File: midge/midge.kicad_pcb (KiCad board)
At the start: 2 copper layers, 121.1 x 83.6 mm, 21 parts, among them SW1 SW_PUSH, SW10 SW_PUSH, SW11 SW_PUSH, SW12 SW_PUSH, SW13 SW_PUSH, SW14 SW_PUSH, SW15 SW_PUSH, SW2 SW_PUSH, SW3 SW_PUSH, SW4 SW_PUSH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

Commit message: Renamed Knott to Midge.
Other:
- board text added: "Midge v0.2.1 https://github.com/jimmerricks/bugs"
- board text removed: "Knott v0.2 https://github.com/jimmerricks/bugs"
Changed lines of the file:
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@@
   (paper "A4")
   (title_block
-    (title "Knott")
-    (date "2021-08-18")
-    (rev "0.2")
+    (title "Midge")
+    (date "2021-09-20")
+    (rev "0.2.1")
     (company "jmnw")
   )
@@
   (gr_line (start 126.027238 50.063266) (end 126.001582 59.553053) (layer "Edge.Cuts") (width 0.15))
   (gr_arc (start 128.001577 59.553052) (end 126.001582 59.553053) (angle -90) (layer "Edge.Cuts") (width 0.15))
-  (gr_text "Knott v0.2\nhttps://github.com/jimmerricks/bugs" (at 139.61 94.87 90) (layer "F.SilkS")
+  (gr_text "Midge v0.2.1\nhttps://github.com/jimmerricks/bugs" (at 139.61 94.87 90) (layer "F.SilkS")
     (effects (font (size 1 1) (thickness 0.12)) (justify left))
   )

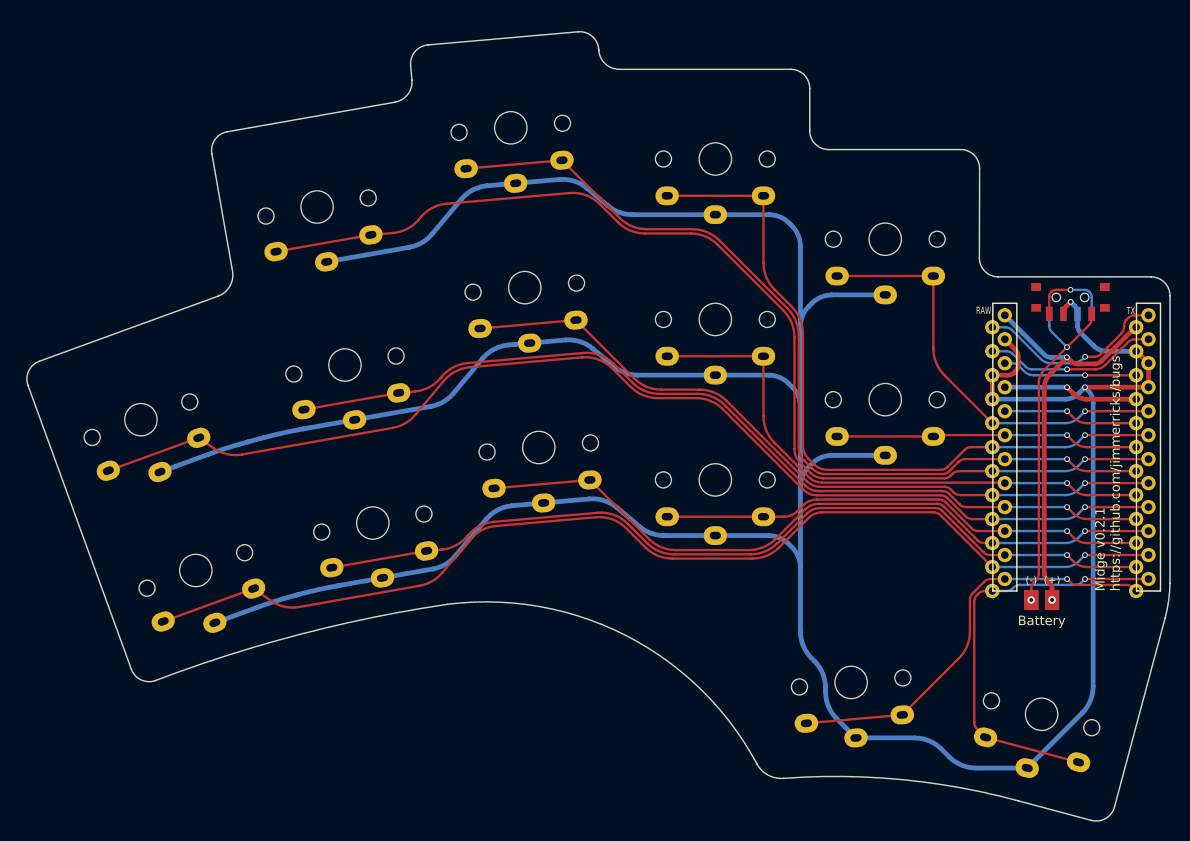
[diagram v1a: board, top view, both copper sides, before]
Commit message: Updated the Midge to the jumper pro micro footprint, breaking the pin order.
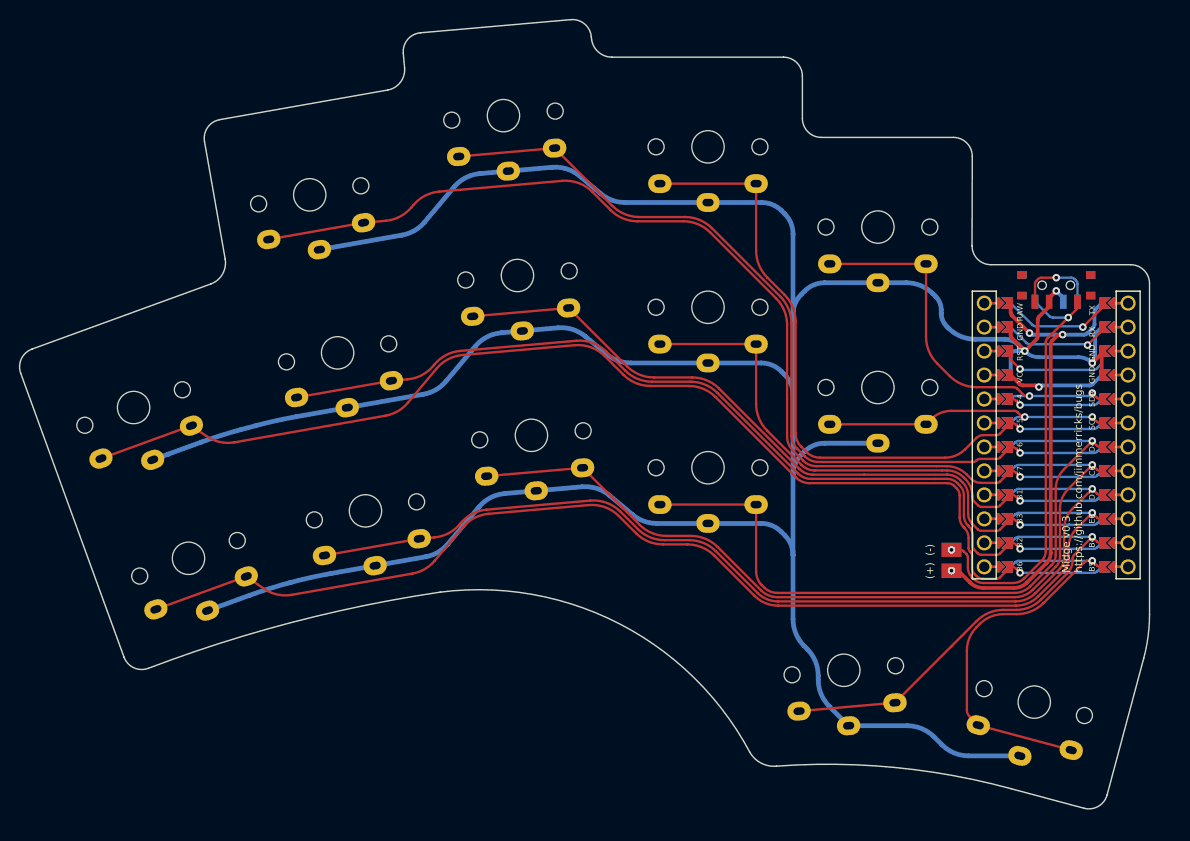
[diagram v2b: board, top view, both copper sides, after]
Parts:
- U1: footprint bugs:ProMicro_reversible -> bugs:ProMicro_jumpers
- moved BT1 10.4 mm to (123.0, 91.6), turned to 90 degrees
- moved U1 2.35 mm to (134.1, 78.3)
- moved PSW1 1.98 mm to (134.1, 62.4)
- moved SW10 1.51 mm to (115.2, 73.3)
- moved Ref** 1.51 mm to (54.3, 66.0)
- moved SW1 1.51 mm to (36.4, 75.4)
- moved SW3 1.51 mm to (75.6, 44.5)
- moved SW5 1.51 mm to (115.2, 56.3)
- moved Ref** 1.51 mm to (57.3, 82.7)
- moved SW6 1.51 mm to (42.2, 91.4)
- moved SW11 1.51 mm to (61.0, 86.3)
- moved SW2 1.51 mm to (55.1, 52.9)
- moved SW9 1.51 mm to (97.2, 64.8)
- moved Ref** 1.51 mm to (112.3, 56.1)
- moved SW13 1.51 mm to (97.2, 81.8)
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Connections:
- U1 pad 10: switch12 -> switch6
- U1 pad 11: switch6 -> switch14
- U1 pad 13: switch14 -> switch1
- U1 pad 14: switch11 -> switch7
- U1 pad 15: switch13 -> switch8
- U1 pad 16: switch7 -> switch9
- U1 pad 17: switch9 -> switch2
- U1 pad 19: switch10 -> switch4
- U1 pad 6: switch4 -> switch10
- U1 pad 7: switch2 -> switch13
- U1 pad 8: switch8 -> switch12
- U1 pad 9: switch1 -> switch11
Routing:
- net GND: track 379.2 -> 344.2 mm, vias 2 -> 3
- net switch13: track 52.1 -> 75.8 mm
- net switch12: track 76.1 -> 89.0 mm
- net switch11: track 92.0 -> 103.8 mm
- net Net-(BT1-Pad2): track 37.0 -> 45.9 mm
- net unconnected-(U1-Pad1): track 20.2 -> 12.0 mm
- net switch6: track 114.2 -> 122.4 mm
- net unconnected-(U1-Pad2): track 18.4 -> 11.4 mm
- net raw: track 44.3 -> 50.8 mm, vias 2 -> 3
- net switch14: track 44.3 -> 48.7 mm
- net unconnected-(U1-Pad20): track 14.3 -> 10.1 mm
- net switch4: track 77.4 -> 73.6 mm
- net VCC: track 14.5 -> 10.9 mm
- net switch1: track 120.9 -> 124.3 mm
- net switch2: track 114.2 -> 110.9 mm
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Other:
- board size 121.1 x 83.6 mm -> 119.7 x 83.6 mm
- board text added: "Midge v0.3 https://github.com/jimmerricks/bugs"
- board text removed: "Midge v0.2.1 https://github.com/jimmerricks/bugs"
